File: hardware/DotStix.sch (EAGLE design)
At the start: 32 parts, among them IC1 CAT24M010TS, IC2 SI1145, U1 ATMEGA328P-MU-QFN32, U2 TMP102, U4 9DoF IMU

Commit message: Modify pullup value for reed, add explanation
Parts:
- R5: value >1MΩ -> 470kΩ
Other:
- note added: "How to calculate the maximum pullup value: The input leakage current needs to be considered, since it is the one dictating the low or high input value of the pin. Typically, it's 1uA. The voltage drop on the pullup, however, should be within the range of 0.6-0.7VDD. Worst case : 1.8V-0.7*1.8V = 0.54V. So we need a minimum drop of 0.54V for the pullup to allow a minimum current to flow into the po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"
- note added: "See sheet #2 for info on how to choose the pullup value."
- note removed: "Using external weak pullup for really low current"
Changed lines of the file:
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@@
 <part name="C9" library="rcl" deviceset="C-EU" device="C0603" value="7pF"/>
 <part name="SUPPLY26" library="supply2" deviceset="GND" device=""/>
-<part name="R5" library="resistor" deviceset="R-EU_" device="R0603" value="&gt;1MΩ"/>
+<part name="R5" library="resistor" deviceset="R-EU_" device="R0603" value="470kΩ"/>
 <part name="+3V8" library="supply1" deviceset="+3V3" device=""/>
 <part name="+3V10" library="supply1" deviceset="+3V3" device=""/>
@@
 <wire x1="312.42" y1="190.5" x2="312.42" y2="109.22" width="0.1524" layer="95" style="longdash"/>
 <text x="364.49" y="163.83" size="1.778" layer="91">Sensor</text>
-<text x="69.85" y="81.28" size="1.778" layer="91">Using external weak pullup for really low current</text>
+<text x="64.77" y="81.28" size="1.778" layer="91">See sheet #2 for info on how to choose the pullup value.</text>
 <text x="407.67" y="171.45" size="1.016" layer="91" align="center">TMP102 or TMP112 (high acc +/-0.5°)</text>
 <wire x1="129.54" y1="-2.54" x2="129.54" y2="-83.82" width="0.1524" layer="95" style="longdash"/>
@@
 </nets>
 </sheet>
+<sheet>
+<plain>
+<text x="2.54" y="5.08" size="1.778" layer="91">How to calculate the maximum pullup value:
+The input leakage current needs to be considered, since it is the one dictating the low or high input value of the pin.
+Typically, it's 1uA.
+The voltage drop on the pullup, however, should be within the range of 0.6-0.7VDD.
+Worst case : 1.8V-0.7*1.8V = 0.54V. So we need a minimum drop of 0.54V for the pullup to allow a minimum
+current to flow into the port at 1uA.
+R = U/I, meaning R=0.54V / 0.000001A = 540kΩ. We can thus opt for 470kΩ.
+Source: https://electronics.stackexchange.com/a/23647/151225</text>
+</plain>
+<instances>
+</instances>
+<busses>
+</busses>
+<nets>
+</nets>
+</sheet>

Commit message: Remove unnecessary solder jumper
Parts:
- removed SJ1: SOLDERJUMPERTRACE, SparkFun:SOLDERJUMPERTRACE
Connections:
- removed net N$5: RN1A.2, SJ1.1
- net +3V3: now also RN1A.2; no longer SJ1.2
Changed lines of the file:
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@@
 <setting verticaltext="up"/>
 </settings>
-<grid distance="0.1" unitdist="inch" unit="inch" style="lines" multiple="1" display="no" altdistance="0.01" altunitdist="inch" altunit="inch"/>
+<grid distance="0.05" unitdist="inch" unit="inch" style="lines" multiple="1" display="no" altdistance="0.01" altunitdist="inch" altunit="inch"/>
 <layers>
 <layer number="1" name="Top" color="4" fill="1" visible="no" active="no"/>
@@
 <part name="+3V11" library="supply1" deviceset="+3V3" device=""/>
 <part name="SUPPLY19" library="supply2" deviceset="GND" device=""/>
-<part name="SJ1" library="SparkFun" deviceset="SOLDERJUMPER" device="TRACE"/>
 <part name="U$3" library="pusbbutton_4x2_5" deviceset="PUSHBUTTON_4X2.5" device=""/>
 <part name="RN1" library="resistor-dil" deviceset="4R-N" device="0402ARV341" value="4.7kΩ"/>
@@
 <instance part="+3V11" gate="G$1" x="97.79" y="156.21"/>
 <instance part="SUPPLY19" gate="GND" x="68.58" y="167.64" rot="R180"/>
-<instance part="SJ1" gate="1" x="88.9" y="148.59"/>
 <instance part="U$3" gate="G$1" x="68.58" y="158.75" rot="R90"/>
 <instance part="RN1" gate="A" x="77.47" y="148.59"/>
@@
 <junction x="97.79" y="138.43"/>
 <wire x1="82.55" y1="133.35" x2="97.79" y2="133.35" width="0.1524" layer="91"/>
-<pinref part="SJ1" gate="1" pin="2"/>
-<wire x1="93.98" y1="148.59" x2="97.79" y2="148.59" width="0.1524" layer="91"/>
 <junction x="97.79" y="148.59"/>
 <pinref part="RN1" gate="B" pin="2"/>
 <pinref part="RN1" gate="C" pin="2"/>
 <pinref part="RN1" gate="D" pin="2"/>
+<pinref part="RN1" gate="A" pin="2"/>
+<wire x1="97.79" y1="148.59" x2="82.55" y2="148.59" width="0.1524" layer="91"/>
 </segment>
 <segment>
@@
 </segment>
 </net>
-<net name="N$5" class="0">
-<segment>
-<pinref part="SJ1" gate="1" pin="1"/>
-<wire x1="83.82" y1="148.59" x2="82.55" y2="148.59" width="0.1524" layer="91"/>
-<pinref part="RN1" gate="A" pin="2"/>
-</segment>
-</net>

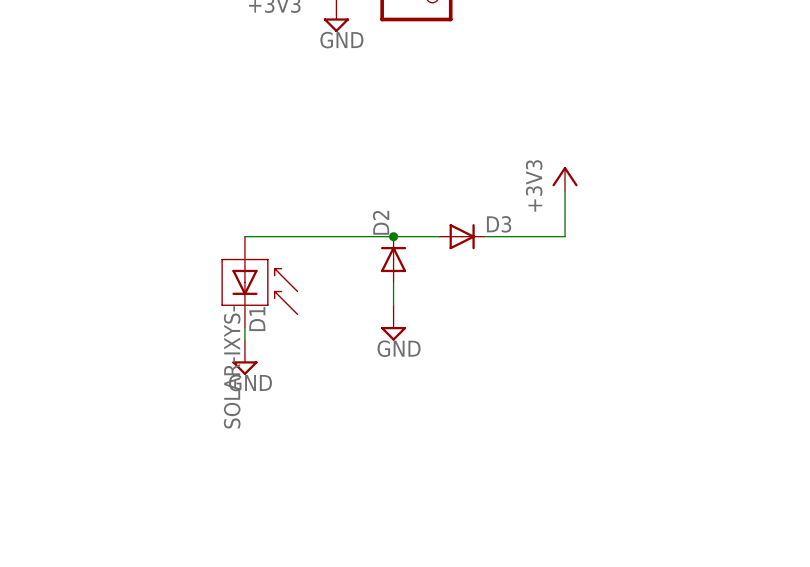
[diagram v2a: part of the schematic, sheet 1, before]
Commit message: Move 3V3 Zener to low side of Schottky
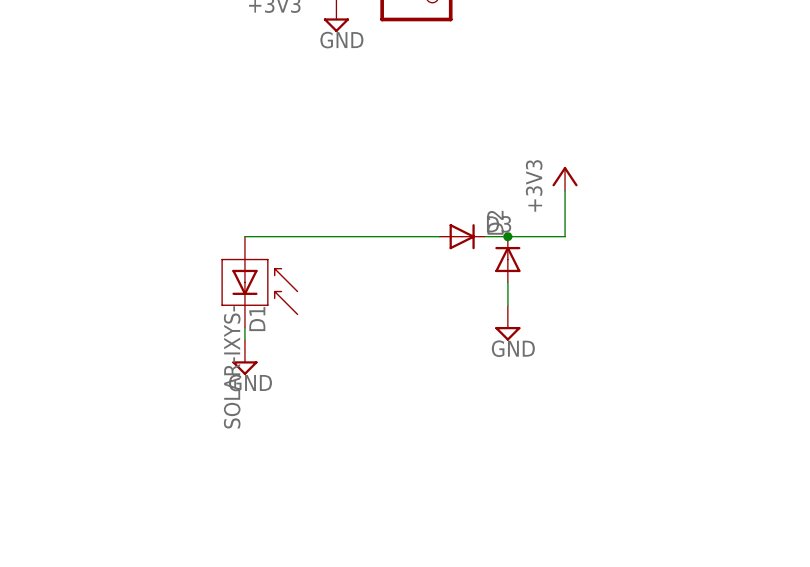
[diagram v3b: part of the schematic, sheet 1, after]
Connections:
- removed net SOLAR_RAW: D1.A, D2.C, D3.A
- new net N$2: D1.A, D3.A
- net +3V3: now also D2.C
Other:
- moved on the sheet: D2
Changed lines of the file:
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@@
 <instance part="SUPPLY5" gate="GND" x="76.2" y="53.34"/>
 <instance part="D1" gate="G$1" x="1.27" y="40.64" rot="R270"/>
-<instance part="D2" gate="G$1" x="17.78" y="43.18" rot="R90"/>
-<instance part="SUPPLY8" gate="GND" x="17.78" y="35.56"/>
+<instance part="D2" gate="G$1" x="30.48" y="43.18" rot="R90"/>
+<instance part="SUPPLY8" gate="GND" x="30.48" y="35.56"/>
 <instance part="D3" gate="G$1" x="25.4" y="45.72"/>
 <instance part="+3V9" gate="G$1" x="36.83" y="53.34"/>
@@
 <pinref part="D2" gate="G$1" pin="A"/>
 <pinref part="SUPPLY8" gate="GND" pin="GND"/>
-<wire x1="17.78" y1="38.1" x2="17.78" y2="40.64" width="0.1524" layer="91"/>
+<wire x1="30.48" y1="40.64" x2="30.48" y2="38.1" width="0.1524" layer="91"/>
 </segment>
 <segment>
@@
 <segment>
 <pinref part="D3" gate="G$1" pin="C"/>
-<wire x1="27.94" y1="45.72" x2="36.83" y2="45.72" width="0.1524" layer="91"/>
+<wire x1="27.94" y1="45.72" x2="30.48" y2="45.72" width="0.1524" layer="91"/>
 <pinref part="+3V9" gate="G$1" pin="+3V3"/>
+<wire x1="30.48" y1="45.72" x2="36.83" y2="45.72" width="0.1524" layer="91"/>
 <wire x1="36.83" y1="50.8" x2="36.83" y2="45.72" width="0.1524" layer="91"/>
+<pinref part="D2" gate="G$1" pin="C"/>
+<junction x="30.48" y="45.72"/>
 </segment>
 <segment>
@@
 </segment>
 </net>
-<net name="SOLAR_RAW" class="0">
-<segment>
-<pinref part="D2" gate="G$1" pin="C"/>
-<wire x1="17.78" y1="45.72" x2="22.86" y2="45.72" width="0.1524" layer="91"/>
-<pinref part="D3" gate="G$1" pin="A"/>
-<pinref part="D1" gate="G$1" pin="A"/>
-<wire x1="1.27" y1="45.72" x2="17.78" y2="45.72" width="0.1524" layer="91"/>
-<junction x="17.78" y="45.72"/>
-</segment>
-</net>
 <net name="LIGHT_SENSE" class="0">
 <segment>
@@
 </segment>
 </net>
+<net name="N$2" class="0">
+<segment>
+<pinref part="D3" gate="G$1" pin="A"/>
+<pinref part="D1" gate="G$1" pin="A"/>
+<wire x1="22.86" y1="45.72" x2="1.27" y2="45.72" width="0.1524" layer="91"/>
+</segment>
+</net>

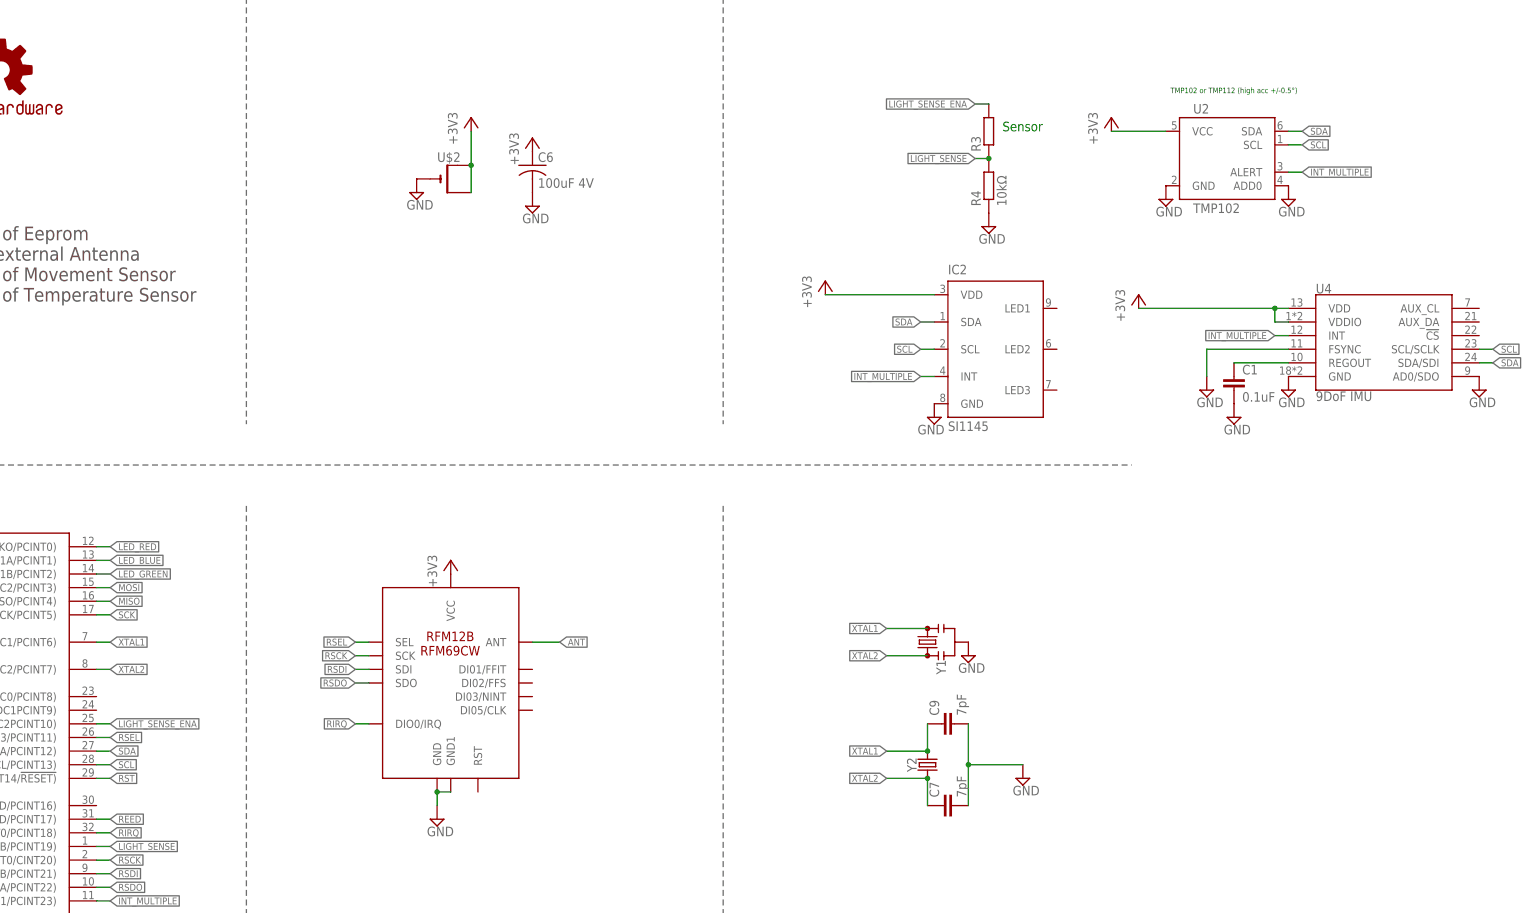
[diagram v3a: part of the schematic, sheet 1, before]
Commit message: Add infos to minimize power
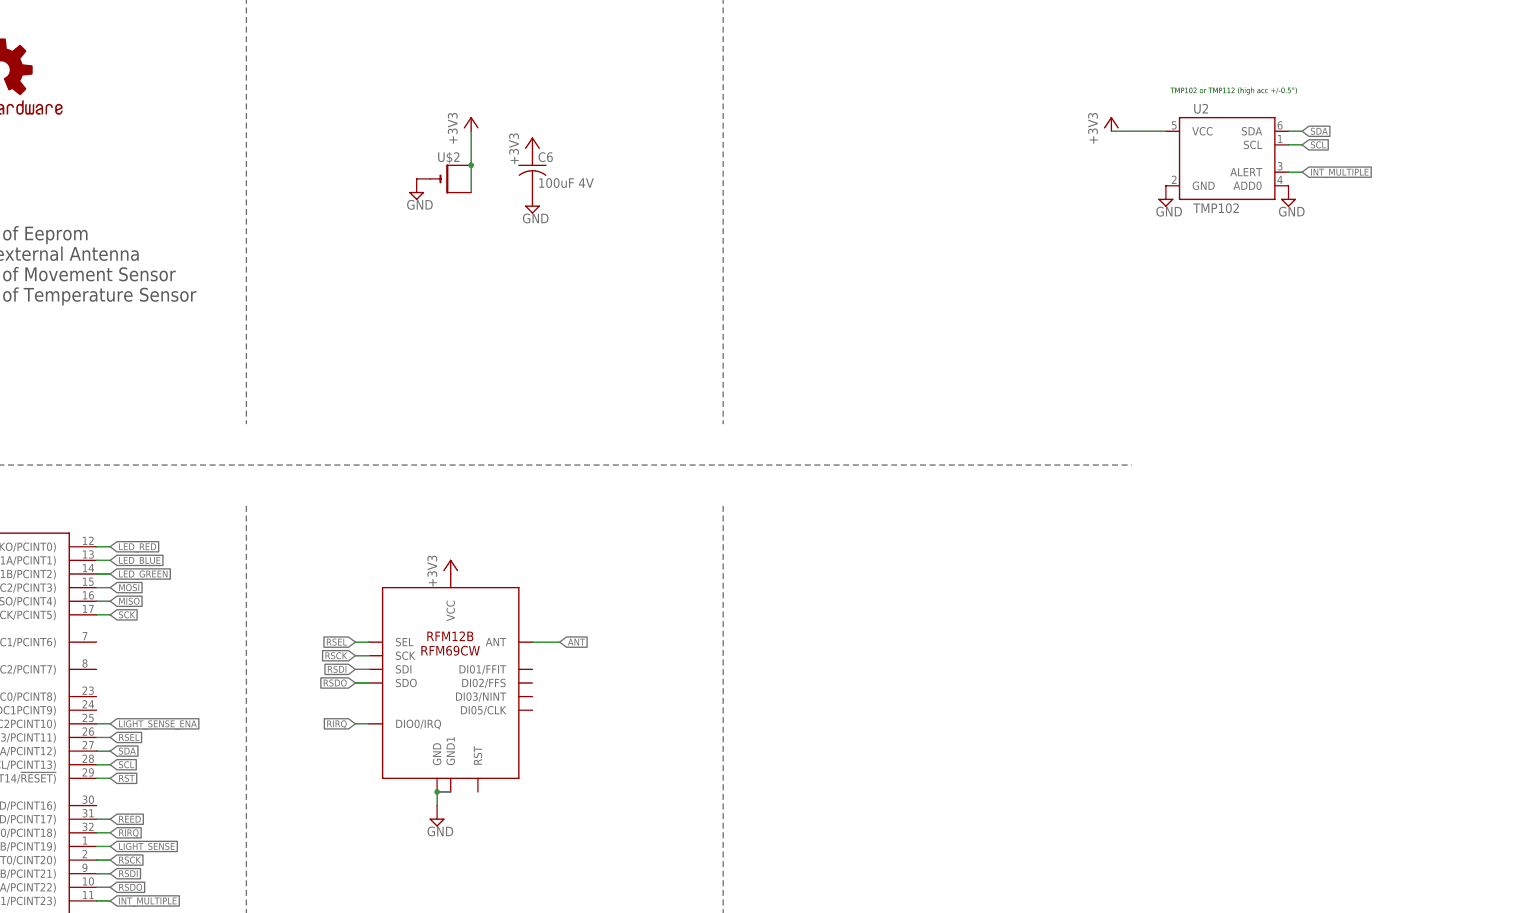
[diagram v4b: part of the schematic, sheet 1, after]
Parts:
- removed C1: 0.1uF, rcl:C-EUC0201
- removed C7, C9: 7pF, rcl:C-EUC0603
- removed IC2: SI1145, silabs:SI1145
- removed R3: (no value), resistor:R-EU_R0805
- removed R4: 10kΩ, resistor:R-EU_R0603
- removed U4: 9DoF IMU, SparkFun-Sensors:MPU-9250
- removed Y1: (no value), SparkFun-Clocks:RESONATORSMD-3.2X1.3
- removed Y2: (no value), SparkFun-Clocks:CRYSTALSMD-3.2X1.5
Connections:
- removed net N$11: C1.1, U4.REGOUT
- removed net XTAL1: C9.1, U1.PB6(XTAL1/TOSC1/PCINT6), Y1.3, Y2.2
- removed net XTAL2: C7.1, U1.PB7(XTAL2/TOSC2/PCINT7), Y1.1, Y2.1
- net +3V3: no longer IC2.VDD, U4.VDD, U4.VDDIO
- net GND: no longer C1.2, C7.2, C9.2, IC2.GND, R4.1, U4.AD0/SDO, U4.FSYNC, U4.GND, Y1.2
- net INT_MULTIPLE: no longer IC2.INT, U4.INT
- net LIGHT_SENSE: no longer R3.1, R4.2
- net LIGHT_SENSE_ENA: no longer R3.2
- net SCL: no longer IC2.SCL, U4.SCL/SCLK
- net SDA: no longer IC2.SDA, U4.SDA/SDI
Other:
- note removed: "Sensor"
